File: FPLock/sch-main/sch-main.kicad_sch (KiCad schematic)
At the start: 48 parts, among them J1 SWD, J4 Touch, SW1 SW_Push, U1 ME54BS01, U2 SN74LVC1G14DBV, U3 AS5600-ASOT, U4 HAL403SO, U5 TC4427AEOA713

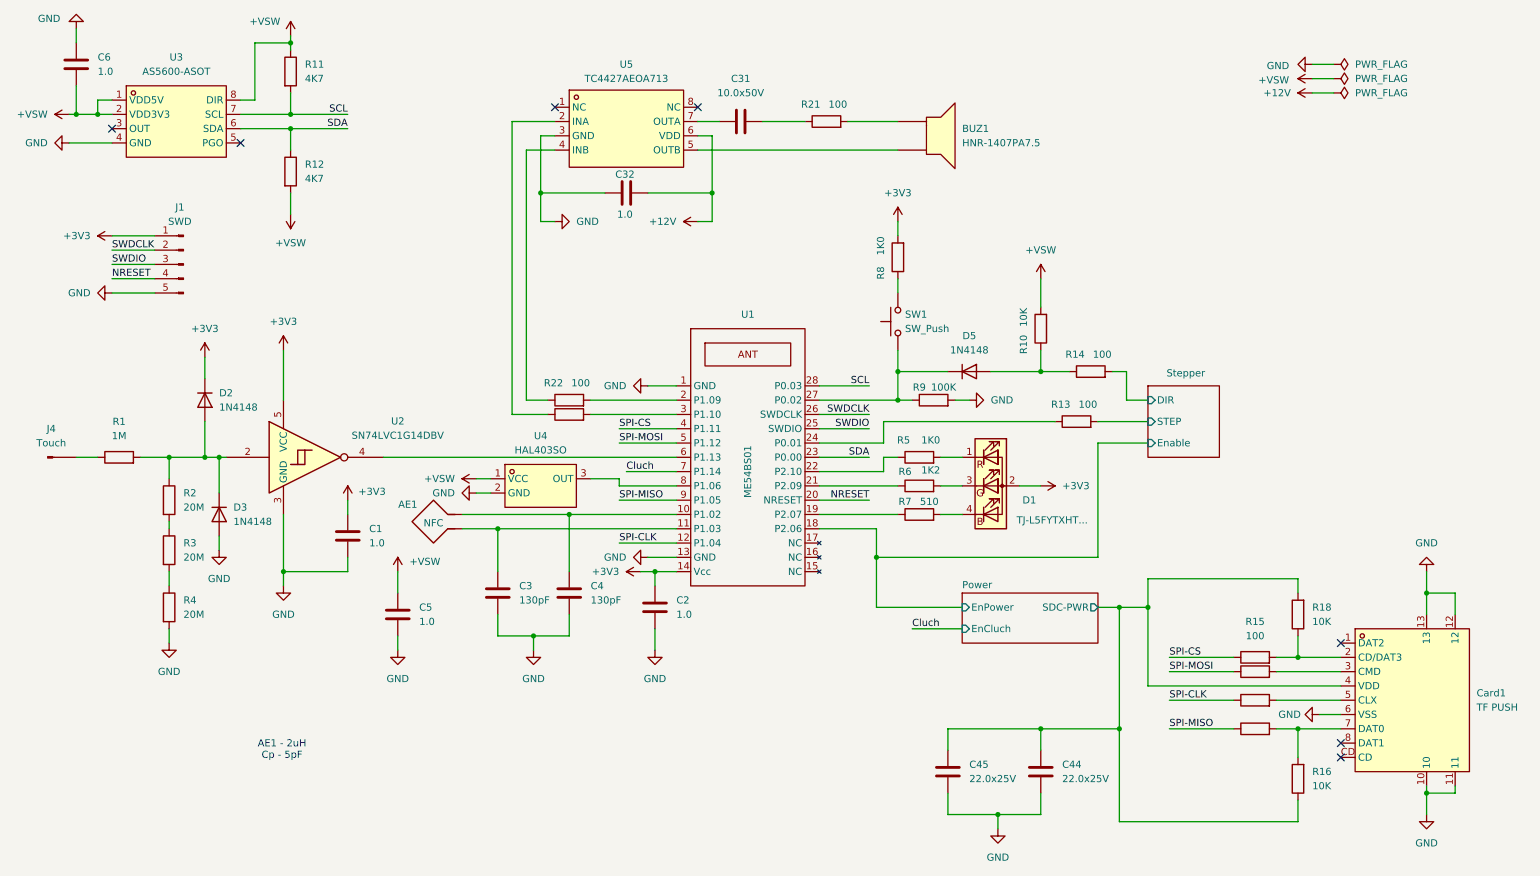
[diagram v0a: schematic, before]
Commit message: Update I2C address
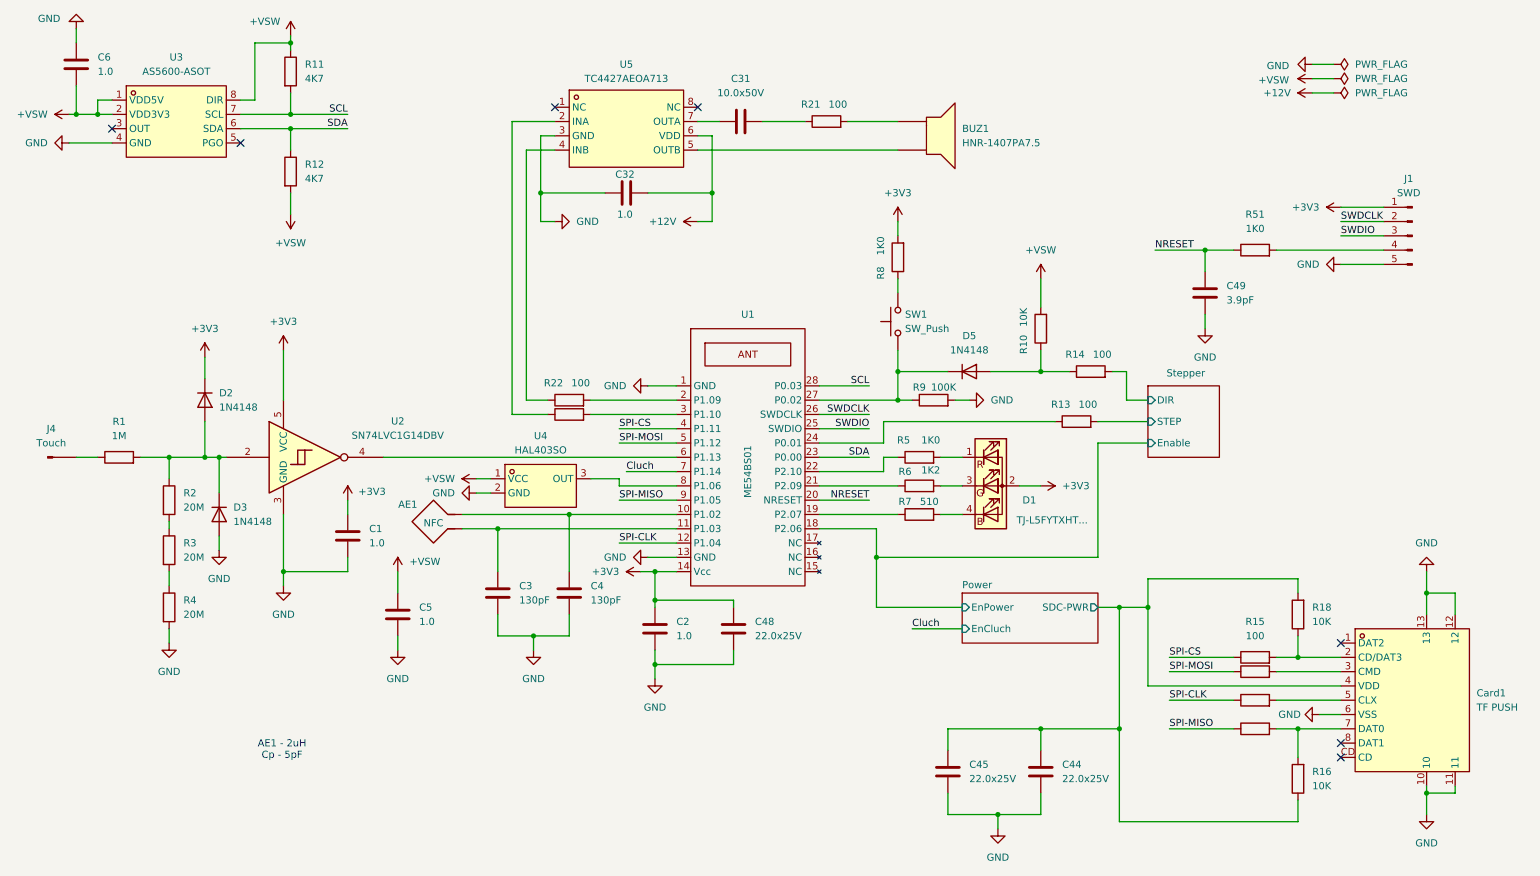
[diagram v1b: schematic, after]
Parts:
- added C48: 22.0x25V, locals:C_1210_3225Metric_Pad1.33x2.70mm_HandSolderExt, symbol Device:C
- added C49: 3.9pF, Capacitor_SMD:C_0603_1608Metric_Pad1.08x0.95mm_HandSolder, symbol Device:C
- added R51: 1K0, Resistor_SMD:R_0603_1608Metric_Pad0.98x0.95mm_HandSolder, symbol Device:R
- C1, C2, C3, C4, C5, C6: footprint (none) -> Capacitor_SMD:C_0603_1608Metric_Pad1.08x0.95mm_HandSolder
- C31: footprint Capacitor_SMD:C_1206_3216Metric_Pad1.33x1.80mm_HandSolder -> locals:C_1206_3216Metric_Pad1.33x1.80mm_HandSolderPlus
- C44, C45: footprint (none) -> locals:C_1210_3225Metric_Pad1.33x2.70mm_HandSolderExt
- D1: footprint (none) -> easyeda2kicad:LED-TH_4P-BD5.8-P1.30
- D2, D3, D5: footprint Diode_THT:D_DO-35_SOD27_P7.62mm_Horizontal -> easyeda2kicad:SOD-80_L3.5-W1.5-RD
- J1: footprint (none) -> Connector_PinHeader_2.54mm:PinHeader_2x03_P2.54mm_Vertical
- J4: footprint (none) -> Connector_PinHeader_2.54mm:PinHeader_1x01_P2.54mm_Vertical
- R1, R10, R11, R12, R13, R14, R21, R22, R23, R5, R6, R7, R8, R9: footprint (none) -> Resistor_SMD:R_0603_1608Metric_Pad0.98x0.95mm_HandSolder
- SW1: footprint (none) -> Button_Switch_THT:SW_PUSH_6mm
- U1: footprint (none) -> ME54BS01:ME54BS01_V1.0
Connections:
- net +3V3: now also C48.1
- net GND: now also C48.2, C49.2
- net NRESET: now also C49.1, R51.1; no longer J1.4 (Pin_4)
- new net: J1.4 (Pin_4), R51.2
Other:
- moved on the sheet: C2, J1
